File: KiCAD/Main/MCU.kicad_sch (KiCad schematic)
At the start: 26 parts, among them Q4 2N7002, SW1 RESET, SW2 USER, U4 STM32H750VBTx, Y2 SiT8008xx-2x-xxE (25MHz)

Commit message: Layout and routing
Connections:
- net Drogue Eject Backup: now also U4.67 (PA8); no longer U4.4 (PE5)
- net Drogue Eject Main: now also U4.68 (PA9); no longer U4.3 (PE4)
- net Main Eject: now also U4.66 (PC9); no longer U4.5 (PE6)
- net SIMU CS1: now also U4.41 (PE11); no longer U4.37 (PE7)
- net SIMU CS3: now also U4.37 (PE7); no longer U4.41 (PE11)
- net SIMU1 INT: now also U4.40 (PE10); no longer U4.36 (PB2)
- net SIMU3 INT: now also U4.36 (PB2); no longer U4.40 (PE10)
- net Servo1_DOut: now also U4.64 (PC7); no longer U4.63 (PC6)
- net Servo2_DOut: now also U4.63 (PC6); no longer U4.64 (PC7)
- net USER_BTN: now also U4.62 (PD15); no longer U4.67 (PA8)
- net USER_LED: now also U4.61 (PD14); no longer U4.66 (PC9)
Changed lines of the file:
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@@
-	(wire
-		(pts
-			(xy 124.46 62.23) (xy 134.62 62.23)
-		)
-		(stroke
-			(width 0)
-			(type default)
-		)
-	)
 	(wire
 		(pts
@@
 	(wire
 		(pts
+			(xy 66.04 143.51) (xy 78.74 143.51)
+		)
+		(stroke
+			(width 0)
+			(type default)
+		)
+	)
+	(wire
+		(pts
 			(xy 115.57 21.59) (xy 127 21.59)
 		)
@@
 	(wire
 		(pts
+			(xy 66.04 146.05) (xy 78.74 146.05)
+		)
+		(stroke
+			(width 0)
+			(type default)
+		)
+	)
+	(wire
+		(pts
 			(xy 104.14 21.59) (xy 104.14 31.75)
 		)
@@
 	(wire
 		(pts
-			(xy 124.46 151.13) (xy 138.43 151.13)
-		)
-		(stroke
-			(width 0)
-			(type default)
-		)
-	)
-	(wire
-		(pts
 			(xy 109.22 21.59) (xy 106.68 21.59)
 		)
@@
 			(width 0)
 			(type default)
+		)
+	)
+	(label "USER_BTN"
+		(at 66.04 146.05 0)
+		(effects
+			(font
+				(size 1.27 1.27)
+			)
+			(justify left bottom)
 		)
 	)
@@
 		)
 	)
-	(label "USER_BTN"
-		(at 134.62 62.23 180)
-		(effects
-			(font
-				(size 1.27 1.27)
-			)
-			(justify right bottom)
+	(label "USER_LED"
+		(at 66.04 143.51 0)
+		(effects
+			(font
+				(size 1.27 1.27)
+			)
+			(justify left bottom)
 		)
 	)
@@
 		)
 	)
-	(label "USER_LED"
-		(at 138.43 151.13 180)
-		(effects
-			(font
-				(size 1.27 1.27)
-			)
-			(justify right bottom)
-		)
-	)
 	(label "BUZZER"
 		(at 231.14 63.5 0)
@@
 			)
 			(justify left bottom)
-		)
-	)
-	(hierarchical_label "Drogue Eject Backup"
-		(shape output)
-		(at 78.74 77.47 180)
-		(effects
-			(font
-				(size 1.27 1.27)
-			)
-			(justify right)
 		)
 	)
@@
 		)
 	)
-	(hierarchical_label "SIMU CS3"
-		(shape output)
-		(at 78.74 92.71 180)
-		(effects
-			(font
-				(size 1.27 1.27)
-			)
-			(justify right)
-		)
-	)
 	(hierarchical_label "USBC_D+"
 		(shape bidirectional)
@@
 		)
 	)
+	(hierarchical_label "Servo1_DOut"
+		(shape output)
+		(at 124.46 146.05 0)
+		(effects
+			(font
+				(size 1.27 1.27)
+			)
+			(justify left)
+		)
+	)
 	(hierarchical_label "Radio RX"
 		(shape input)
@@
 		)
 	)
-	(hierarchical_label "SIMU CS1"
-		(shape output)
-		(at 78.74 82.55 180)
-		(effects
-			(font
-				(size 1.27 1.27)
-			)
-			(justify right)
-		)
-	)
 	(hierarchical_label "SD_MISO"
 		(shape input)
@@
 		)
 	)
+	(hierarchical_label "Servo2_DOut"
+		(shape output)
+		(at 124.46 143.51 0)
+		(effects
+			(font
+				(size 1.27 1.27)
+			)
+			(justify left)
+		)
+	)
 	(hierarchical_label "SHT41 SCL"
 		(shape output)
@@
 		)
 	)
-	(hierarchical_label "SIMU1 INT"
-		(shape input)
-		(at 124.46 90.17 0)
-		(effects
-			(font
-				(size 1.27 1.27)
-			)
-			(justify left)
+	(hierarchical_label "SIMU CS3"
+		(shape output)
+		(at 78.74 82.55 180)
+		(effects
+			(font
+				(size 1.27 1.27)
+			)
+			(justify right)
 		)
 	)
@@
 		)
 	)
+	(hierarchical_label "SIMU1 INT"
+		(shape input)
+		(at 78.74 90.17 180)
+		(effects
+			(font
+				(size 1.27 1.27)
+			)
+			(justify right)
+		)
+	)
 	(hierarchical_label "DEBUG_JTMS-SWCLK"
 		(shape input)
@@
 		)
 	)
+	(hierarchical_label "Drogue Eject Main"
+		(shape output)
+		(at 124.46 64.77 0)
+		(effects
+			(font
+				(size 1.27 1.27)
+			)
+			(justify left)
+		)
+	)
 	(hierarchical_label "SD CS"
 		(shape output)
@@
 		)
 	)
-	(hierarchical_label "Servo2_DOut"
-		(shape output)
-		(at 124.46 146.05 0)
-		(effects
-			(font
-				(size 1.27 1.27)
-			)
-			(justify left)
-		)
-	)
-	(hierarchical_label "Drogue Eject Main"
-		(shape output)
-		(at 78.74 74.93 180)
-		(effects
-			(font
-				(size 1.27 1.27)
-			)
-			(justify right)
-		)
-	)
 	(hierarchical_label "GPS SCL"
 		(shape output)
@@
 		)
 	)
+	(hierarchical_label "Main Eject"
+		(shape output)
+		(at 124.46 151.13 0)
+		(effects
+			(font
+				(size 1.27 1.27)
+			)
+			(justify left)
+		)
+	)
 	(hierarchical_label "MOSI2_ISM"
 		(shape input)
@@
 		)
 	)
-	(hierarchical_label "Main Eject"
+	(hierarchical_label "SIMU CS1"
 		(shape output)
-		(at 78.74 80.01 180)
+		(at 78.74 92.71 180)
 		(effects
 			(font
@@
 			)
 			(justify right)
-		)
-	)
-	(hierarchical_label "Servo1_DOut"
-		(shape output)
-		(at 124.46 143.51 0)
-		(effects
-			(font
-				(size 1.27 1.27)
-			)
-			(justify left)
 		)
 	)
@@
 		)
 	)
+	(hierarchical_label "Drogue Eject Backup"
+		(shape output)
+		(at 124.46 62.23 0)
+		(effects
+			(font
+				(size 1.27 1.27)
+			)
+			(justify left)
+		)
+	)
 	(hierarchical_label "SIMU3 INT"
 		(shape input)
-		(at 78.74 90.17 180)
-		(effects
-			(font
-				(size 1.27 1.27)
-			)
-			(justify right)
+		(at 124.46 90.17 0)
+		(effects
+			(font
+				(size 1.27 1.27)
+			)
+			(justify left)
 		)
 	)
@@
 		(lib_id "Device:C")
 		(at 194.31 25.4 0)
+		(mirror y)
 		(unit 1)
 		(exclude_from_sim no)
@@
 		(on_board yes)
 		(dnp no)
-		(fields_autoplaced yes)
 		(property "Reference" "C14"
-			(at 198.12 24.13 0)
+			(at 190.5 24.13 0)
 			(effects
 				(font
@@
 		)
 		(property "Value" "4.7u"
-			(at 198.12 26.67 0)
+			(at 190.5 26.67 0)
 			(effects
 				(font
@@
 		)
 		(property "Footprint" "Capacitor_SMD:C_0603_1608Metric"
-			(at 195.2752 29.21 0)
-			(effects
-				(font
+			(at 193.3448 29.21 0)
+			(effects
+				(font

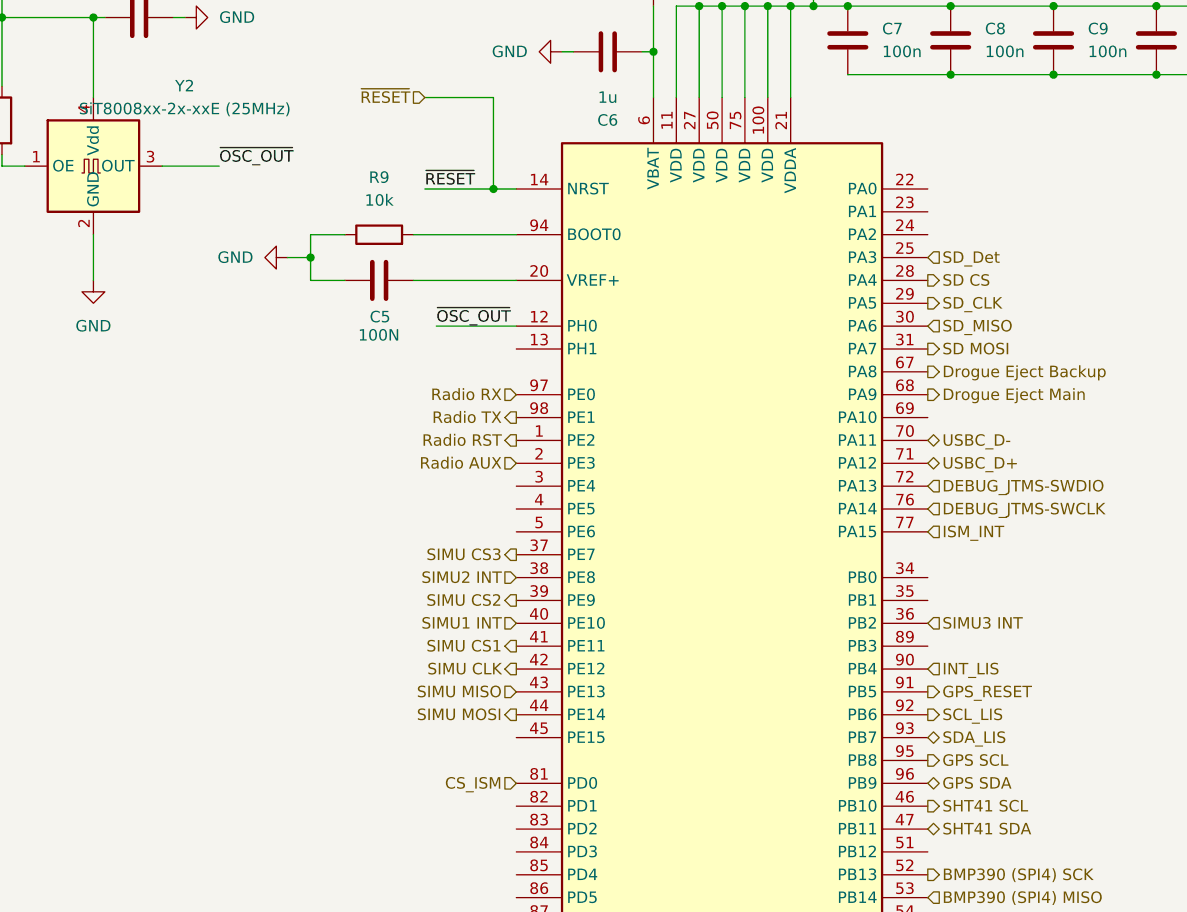
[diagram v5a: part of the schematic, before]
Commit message: Update aux magnetometer, test THs, and silkscreens
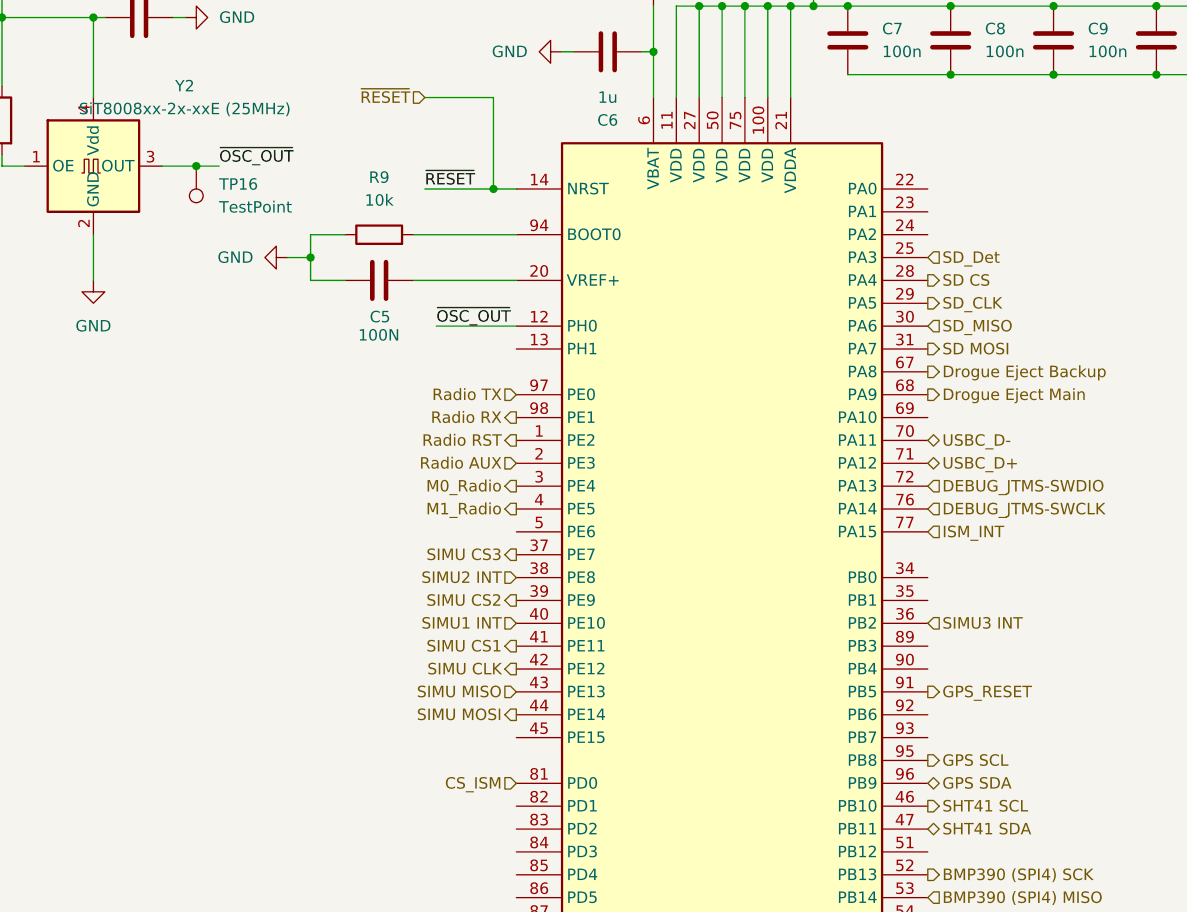
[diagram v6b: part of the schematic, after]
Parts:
- added TP16: TestPoint, TestPoint:TestPoint_THTPad_1.5x1.5mm_Drill0.7mm, symbol Connector:TestPoint
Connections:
- net Radio RX: now also U4.98 (PE1); no longer U4.97 (PE0)
- net Radio TX: now also U4.97 (PE0); no longer U4.98 (PE1)
- net ~{OSC_OUT}: now also TP16.1
- net M0_Radio: now reaches U4.3 (PE4)
- net M1_Radio: now reaches U4.4 (PE5)
- net INT_LIS: no longer names the net of U4.90 (PB4)
- net SCL_LIS: no longer names the net of U4.92 (PB6)
- net SDA_LIS: no longer names the net of U4.93 (PB7)
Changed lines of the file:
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@@
+	)
+	(junction
+		(at 43.18 39.37)
+		(diameter 0)
+		(color 0 0 0 0)
 	)
 	(junction
@@
 	(wire
 		(pts
+			(xy 43.18 39.37) (xy 45.72 39.37)
+		)
+		(stroke
+			(width 0)
+			(type default)
+		)
+	)
+	(wire
+		(pts
 			(xy 92.71 26.67) (xy 93.98 26.67)
 		)
@@
 	(wire
 		(pts
-			(xy 39.37 39.37) (xy 45.72 39.37)
+			(xy 39.37 39.37) (xy 43.18 39.37)
 		)
 		(stroke
@@
 			)
 			(justify left bottom)
+		)
+	)
+	(hierarchical_label "M0_Radio"
+		(shape output)
+		(at 78.74 74.93 180)
+		(effects
+			(font
+				(size 1.27 1.27)
+			)
+			(justify right)
 		)
 	)
@@
 		)
 	)
-	(hierarchical_label "SCL_LIS"
-		(shape output)
-		(at 124.46 100.33 0)
-		(effects
-			(font
-				(size 1.27 1.27)
-			)
-			(justify left)
-		)
-	)
 	(hierarchical_label "GPS SDA"
 		(shape bidirectional)
@@
 	)
 	(hierarchical_label "Radio TX"
+		(shape input)
+		(at 78.74 64.77 180)
+		(effects
+			(font
+				(size 1.27 1.27)
+			)
+			(justify right)
+		)
+	)
+	(hierarchical_label "BMP390 INT3"
+		(shape input)
+		(at 78.74 140.97 180)
+		(effects
+			(font
+				(size 1.27 1.27)
+			)
+			(justify right)
+		)
+	)
+	(hierarchical_label "Servo1_DOut"
+		(shape output)
+		(at 124.46 146.05 0)
+		(effects
+			(font
+				(size 1.27 1.27)
+			)
+			(justify left)
+		)
+	)
+	(hierarchical_label "SD_MISO"
+		(shape input)
+		(at 124.46 57.15 0)
+		(effects
+			(font
+				(size 1.27 1.27)
+			)
+			(justify left)
+		)
+	)
+	(hierarchical_label "SCK2_ISM"
+		(shape input)
+		(at 124.46 153.67 0)
+		(effects
+			(font
+				(size 1.27 1.27)
+			)
+			(justify left)
+		)
+	)
+	(hierarchical_label "BMP390 (SPI4) MISO"
+		(shape input)
+		(at 124.46 120.65 0)
+		(effects
+			(font
+				(size 1.27 1.27)
+			)
+			(justify left)
+		)
+	)
+	(hierarchical_label "Servo2_DOut"
+		(shape output)
+		(at 124.46 143.51 0)
+		(effects
+			(font
+				(size 1.27 1.27)
+			)
+			(justify left)
+		)
+	)
+	(hierarchical_label "SHT41 SCL"
+		(shape output)
+		(at 124.46 110.49 0)
+		(effects
+			(font
+				(size 1.27 1.27)
+			)
+			(justify left)
+		)
+	)
+	(hierarchical_label "BMP390 (SPI4) CS3"
+		(shape output)
+		(at 78.74 138.43 180)
+		(effects
+			(font
+				(size 1.27 1.27)
+			)
+			(justify right)
+		)
+	)
+	(hierarchical_label "Servo1_Encoder"
+		(shape input)
+		(at 124.46 133.35 0)
+		(effects
+			(font
+				(size 1.27 1.27)
+			)
+			(justify left)
+		)
+	)
+	(hierarchical_label "SIMU CS3"
+		(shape output)
+		(at 78.74 82.55 180)
+		(effects
+			(font
+				(size 1.27 1.27)
+			)
+			(justify right)
+		)
+	)
+	(hierarchical_label "SIMU MISO"
+		(shape input)
+		(at 78.74 97.79 180)
+		(effects
+			(font
+				(size 1.27 1.27)
+			)
+			(justify right)
+		)
+	)
+	(hierarchical_label "Radio AUX"
+		(shape input)
+		(at 78.74 72.39 180)
+		(effects
+			(font
+				(size 1.27 1.27)
+			)
+			(justify right)
+		)
+	)
+	(hierarchical_label "BMP390 (SPI4) CS1"
+		(shape output)
+		(at 78.74 128.27 180)
+		(effects
+			(font
+				(size 1.27 1.27)
+			)
+			(justify right)
+		)
+	)
+	(hierarchical_label "Radio RX"
 		(shape output)
 		(at 78.74 67.31 180)
@@
 		)
 	)
-	(hierarchical_label "BMP390 INT3"
-		(shape input)
-		(at 78.74 140.97 180)
-		(effects
-			(font
-				(size 1.27 1.27)
-			)
-			(justify right)
-		)
-	)
-	(hierarchical_label "Servo1_DOut"
-		(shape output)
-		(at 124.46 146.05 0)
-		(effects
-			(font
-				(size 1.27 1.27)
-			)
-			(justify left)
-		)
-	)
-	(hierarchical_label "Radio RX"
-		(shape input)
-		(at 78.74 64.77 180)
-		(effects
-			(font
-				(size 1.27 1.27)
-			)
-			(justify right)
-		)
-	)
-	(hierarchical_label "SD_MISO"
-		(shape input)
-		(at 124.46 57.15 0)
-		(effects
-			(font
-				(size 1.27 1.27)
-			)
-			(justify left)
-		)
-	)
-	(hierarchical_label "SCK2_ISM"
-		(shape input)
-		(at 124.46 153.67 0)
-		(effects
-			(font
-				(size 1.27 1.27)
-			)
-			(justify left)
-		)
-	)
-	(hierarchical_label "BMP390 (SPI4) MISO"
-		(shape input)
-		(at 124.46 120.65 0)
-		(effects
-			(font
-				(size 1.27 1.27)
-			)
-			(justify left)
-		)
-	)
-	(hierarchical_label "Servo2_DOut"
-		(shape output)
-		(at 124.46 143.51 0)
-		(effects
-			(font
-				(size 1.27 1.27)
-			)
-			(justify left)
-		)
-	)
-	(hierarchical_label "SHT41 SCL"
-		(shape output)
-		(at 124.46 110.49 0)
-		(effects
-			(font
-				(size 1.27 1.27)
-			)
-			(justify left)
-		)
-	)
-	(hierarchical_label "BMP390 (SPI4) CS3"
-		(shape output)
-		(at 78.74 138.43 180)
-		(effects
-			(font
-				(size 1.27 1.27)
-			)
-			(justify right)
-		)
-	)
-	(hierarchical_label "Servo1_Encoder"
-		(shape input)
-		(at 124.46 133.35 0)
-		(effects
-			(font
-				(size 1.27 1.27)
-			)
-			(justify left)
-		)
-	)
-	(hierarchical_label "INT_LIS"
-		(shape input)
-		(at 124.46 95.25 0)
-		(effects
-			(font
-				(size 1.27 1.27)
-			)
-			(justify left)
-		)
-	)
-	(hierarchical_label "SIMU CS3"
-		(shape output)
-		(at 78.74 82.55 180)
-		(effects
-			(font
-				(size 1.27 1.27)
-			)
-			(justify right)
-		)
-	)
-	(hierarchical_label "SIMU MISO"
-		(shape input)
-		(at 78.74 97.79 180)
-		(effects
-			(font
-				(size 1.27 1.27)
-			)
-			(justify right)
-		)
-	)
-	(hierarchical_label "Radio AUX"
-		(shape input)
-		(at 78.74 72.39 180)
-		(effects
-			(font
-				(size 1.27 1.27)
-			)
-			(justify right)
-		)
-	)
-	(hierarchical_label "BMP390 (SPI4) CS1"
-		(shape output)
-		(at 78.74 128.27 180)
-		(effects
-			(font
-				(size 1.27 1.27)
-			)
-			(justify right)
-		)
-	)
 	(hierarchical_label "SIMU1 INT"
 		(shape input)
@@
 			)
 			(justify left)
+		)
+	)
+	(hierarchical_label "M1_Radio"
+		(shape output)
+		(at 78.74 77.47 180)
+		(effects
+			(font
+				(size 1.27 1.27)
+			)
+			(justify right)
 		)
 	)
@@
 			)
 			(justify right)
-		)
-	)
-	(hierarchical_label "SDA_LIS"
-		(shape bidirectional)
-		(at 124.46 102.87 0)
-		(effects
-			(font
-				(size 1.27 1.27)
-			)
-			(justify left)
 		)
 	)
@@
 					(unit 1)
 				)
+			)
+		)
+	)
+	(symbol
+		(lib_id "Connector:TestPoint")
+		(at 43.18 39.37 180)
+		(unit 1)
+		(exclude_from_sim no)
+		(in_bom yes)
+		(on_board yes)
+		(dnp no)
+		(fields_autoplaced yes)
+		(property "Reference" "TP16"
+			(at 45.72 41.4019 0)
+			(effects
+				(font
+					(size 1.27 1.27)
+				)
+				(justify right)
+			)
+		)
+		(property "Value" "TestPoint"
+			(at 45.72 43.9419 0)
+			(effects
+				(font
+					(size 1.27 1.27)
+				)
+				(justify right)
+			)
+		)
+		(property "Footprint" "TestPoint:TestPoint_THTPad_1.5x1.5mm_Drill0.7mm"
+			(at 38.1 39.37 0)
+			(effects
+				(font
+					(size 1.27 1.27)
+				)
+				(hide yes)
+			)
+		)
+		(property "Datasheet" "~"
+			(at 38.1 39.37 0)
+			(effects
+				(font
+					(size 1.27 1.27)
+				)
+				(hide yes)
+			)
+		)
+		(property "Description" "test point"
+			(at 43.18 39.37 0)
+			(effects
+				(font
+					(size 1.27 1.27)
+				)
+				(hide yes)
+			)
+		)
+		(pin "1"
+		)
+		(instances
+			(project ""
+				(path "/bbb10697-a5dd-43b8-9c6f-4c5919cf3463/370a154e-a6dd-4f7c-9f86-560fca4820f6"
+					(reference "TP16")
+					(unit 1)
+				)
